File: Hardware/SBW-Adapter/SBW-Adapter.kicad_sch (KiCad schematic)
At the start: 5 parts, among them J1 JTAG, J2 SpyBiWire, SW1 SW_SPDT

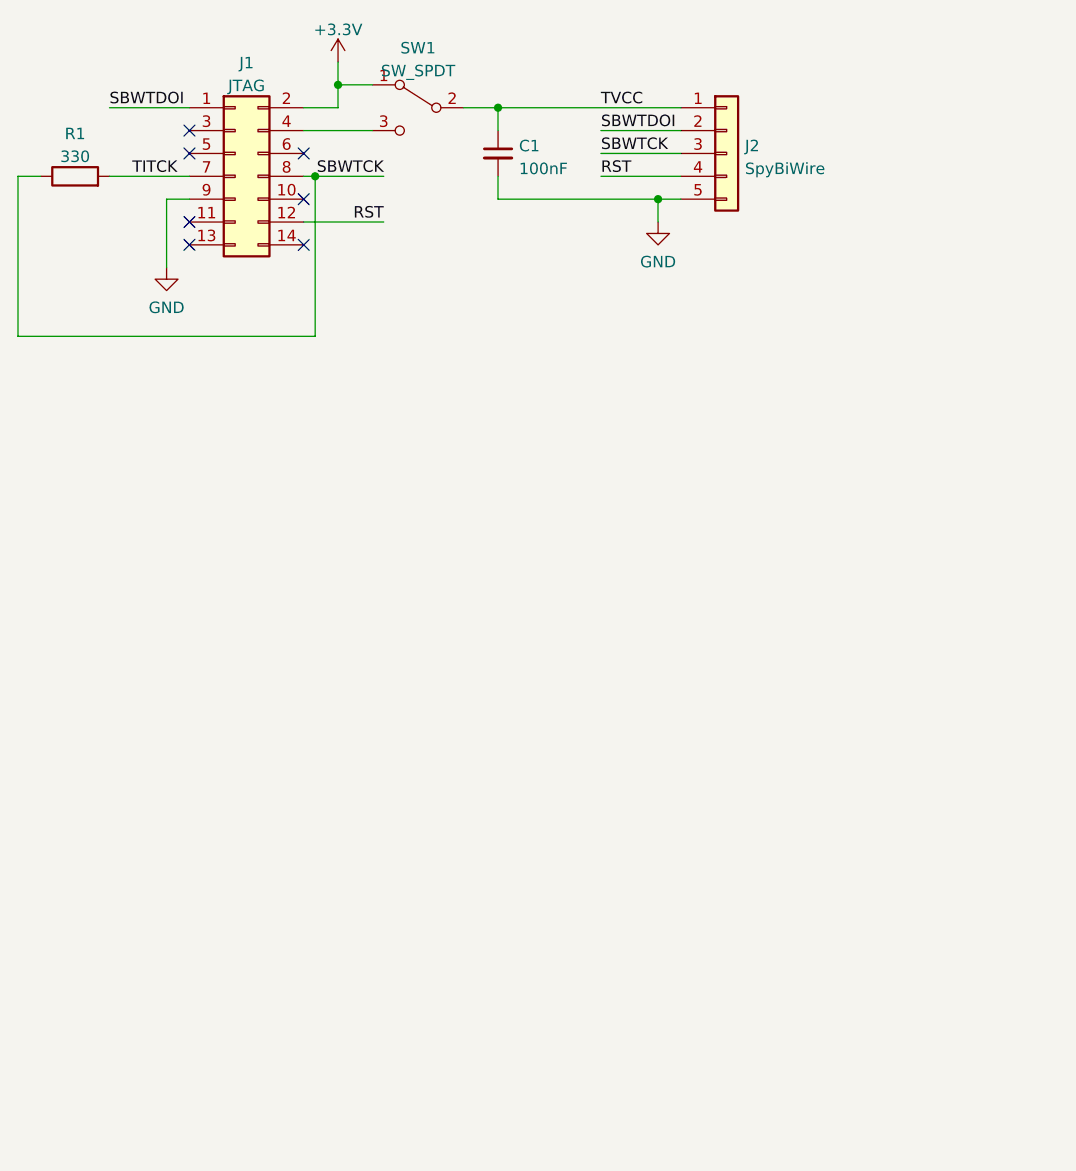
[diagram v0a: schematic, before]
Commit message: Files for PCB Manufacturing of 4 boards. Preparation for Board documentation
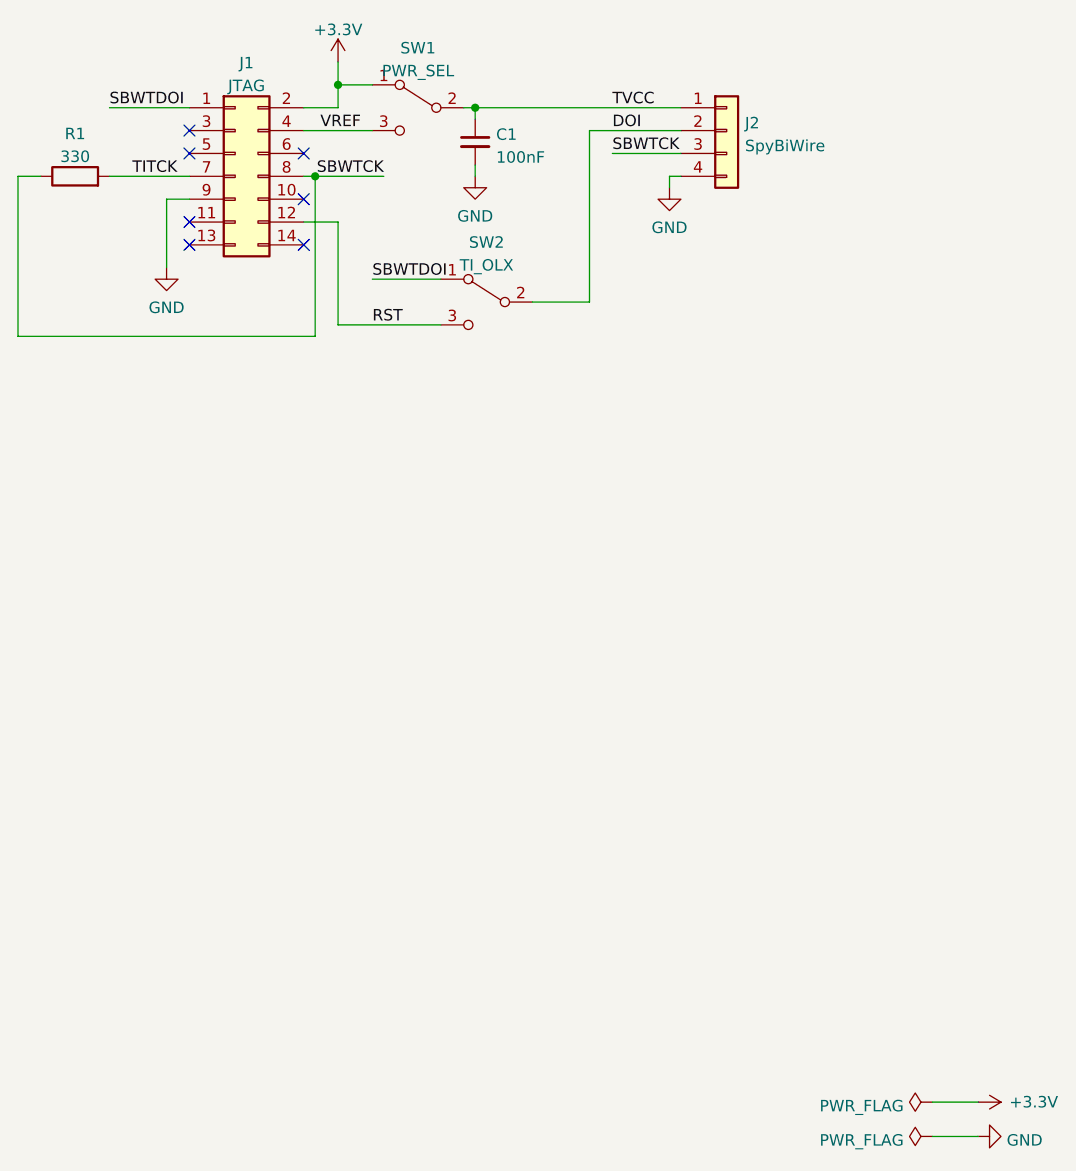
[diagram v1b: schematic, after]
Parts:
- added SW2: TI_OLX, Button_Switch_SMD:SW_SPDT_PCM12, symbol Switch:SW_SPDT
- J2: footprint Connector_PinHeader_2.54mm:PinHeader_1x05_P2.54mm_Horizontal -> Connector_JST:JST_XH_B4B-XH-A_1x04_P2.50mm_Vertical; symbol Connector_Generic:Conn_01x05 -> Connector_Generic:Conn_01x04
- SW1: value SW_SPDT -> PWR_SEL
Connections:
- net GND: now also J2.4 (Pin_4); no longer J2.5 (Pin_5)
- net RST: now also SW2.3 (C); no longer J2.4 (Pin_4)
- net SBWTDOI: now also SW2.1 (A); no longer J2.2 (Pin_2)
- net VREF: now reaches J1.4 (Pin_4), SW1.3 (C)
- new net DOI: J2.2 (Pin_2), SW2.2 (B)
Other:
- moved on the sheet: C1

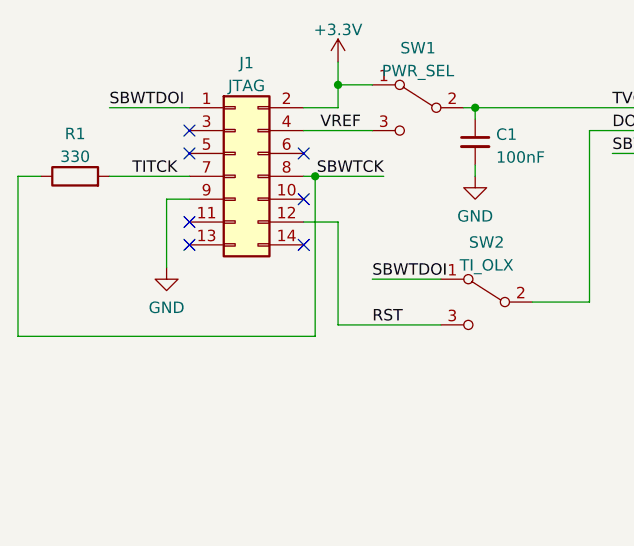
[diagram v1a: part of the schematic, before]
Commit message: Fixed an error on the Olimex SBW layout
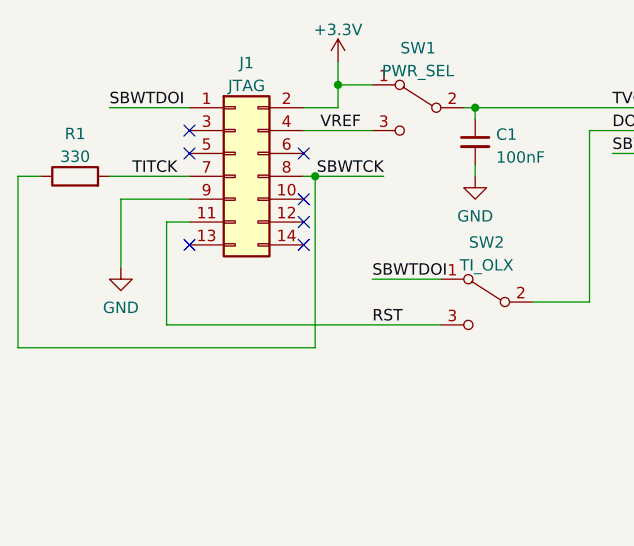
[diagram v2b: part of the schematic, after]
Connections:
- net RST: now also J1.11 (Pin_11); no longer J1.12 (Pin_12)
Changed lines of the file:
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@@
 (kicad_sch (version 20211123) (generator eeschema)
   (paper "A4")
+  (title_block
+    (date "2022-09-06")
+    (rev "2")
+  )
   (junction (at 87.63 85.09) (diameter 0) (color 0 0 0 0)
   )
@@
   )
   (no_connect (at 86.36 82.55))
+  (no_connect (at 86.36 90.17))
   (no_connect (at 86.36 87.63))
   (no_connect (at 86.36 92.71))
-  (no_connect (at 73.66 90.17))
   (no_connect (at 73.66 82.55))
   (no_connect (at 73.66 92.71))
@@
     (stroke (width 0) (type default) (color 0 0 0 0))
   )
+  (wire (pts (xy 71.12 101.6) (xy 101.6 101.6))
+    (stroke (width 0) (type default) (color 0 0 0 0))
+  )
   (wire (pts (xy 127 85.09) (xy 127 86.36))
     (stroke (width 0) (type default) (color 0 0 0 0))
@@
     (stroke (width 0) (type default) (color 0 0 0 0))
   )
-  (wire (pts (xy 73.66 87.63) (xy 71.12 87.63))
-    (stroke (width 0) (type default) (color 0 0 0 0))
-  )
-  (wire (pts (xy 54.61 102.87) (xy 54.61 85.09))
-    (stroke (width 0) (type default) (color 0 0 0 0))
-  )
-  (wire (pts (xy 87.63 102.87) (xy 54.61 102.87))
+  (wire (pts (xy 73.66 87.63) (xy 66.04 87.63))
+    (stroke (width 0) (type default) (color 0 0 0 0))
+  )
+  (wire (pts (xy 54.61 104.14) (xy 54.61 85.09))
+    (stroke (width 0) (type default) (color 0 0 0 0))
+  )
+  (wire (pts (xy 87.63 104.14) (xy 54.61 104.14))
     (stroke (width 0) (type default) (color 0 0 0 0))
   )
@@
     (stroke (width 0) (type default) (color 0 0 0 0))
   )
-  (wire (pts (xy 101.6 101.6) (xy 90.17 101.6))
-    (stroke (width 0) (type default) (color 0 0 0 0))
-  )
   (wire (pts (xy 90.17 74.93) (xy 93.98 74.93))
     (stroke (width 0) (type default) (color 0 0 0 0))
   )
-  (wire (pts (xy 86.36 90.17) (xy 90.17 90.17))
+  (wire (pts (xy 71.12 101.6) (xy 71.12 90.17))
     (stroke (width 0) (type default) (color 0 0 0 0))
   )
@@
     (stroke (width 0) (type default) (color 0 0 0 0))
   )
-  (wire (pts (xy 87.63 85.09) (xy 87.63 102.87))
-    (stroke (width 0) (type default) (color 0 0 0 0))
-  )
-  (wire (pts (xy 90.17 90.17) (xy 90.17 101.6))
+  (wire (pts (xy 87.63 85.09) (xy 87.63 104.14))
+    (stroke (width 0) (type default) (color 0 0 0 0))
+  )
+  (wire (pts (xy 71.12 90.17) (xy 73.66 90.17))
     (stroke (width 0) (type default) (color 0 0 0 0))
   )
@@
     (stroke (width 0) (type default) (color 0 0 0 0))
   )
-  (wire (pts (xy 71.12 87.63) (xy 71.12 95.25))
+  (wire (pts (xy 66.04 87.63) (xy 66.04 95.25))
     (stroke (width 0) (type default) (color 0 0 0 0))
   )
@@
     (pin "3")
   )
-  (symbol (lib_id "power:GND") (at 71.12 95.25 0) (unit 1)
-    (in_bom yes) (on_board yes) (fields_autoplaced)
-    (property "Reference" "#PWR0101" (id 0) (at 71.12 101.6 0)
-      (effects (font (size 1.27 1.27)) hide)
-    )
-    (property "Value" "GND" (id 1) (at 71.12 99.6934 0))
-    (property "Footprint" "" (id 2) (at 71.12 95.25 0)
-      (effects (font (size 1.27 1.27)) hide)
-    )
-    (property "Datasheet" "" (id 3) (at 71.12 95.25 0)
-      (effects (font (size 1.27 1.27)) hide)
-    )
+  (symbol (lib_id "power:GND") (at 66.04 95.25 0) (unit 1)
+    (in_bom yes) (on_board yes) (fields_autoplaced)
+    (property "Reference" "#PWR0101" (id 0) (at 66.04 101.6 0)
+      (effects (font (size 1.27 1.27)) hide)
+    )
+    (property "Value" "GND" (id 1) (at 66.04 99.6934 0))
+    (property "Footprint" "" (id 2) (at 66.04 95.25 0)
+      (effects (font (size 1.27 1.27)) hide)
+    )
+    (property "Datasheet" "" (id 3) (at 66.04 95.25 0)
+      (effects (font (size 1.27 1.27)) hide)
+    )

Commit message: Review of SBW-Adapter
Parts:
- SW1, SW2: footprint Button_Switch_SMD:SW_SPDT_PCM12 -> lib:SW_SPDT_PCM12; symbol Switch:SW_SPDT -> SW_SPDT_PCM12:SW_SPDT_PCM12
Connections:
- net GND: now also SW1.4 (GND), SW2.4 (GND)
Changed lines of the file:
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@@
   (paper "A4")
   (title_block
-    (date "2022-09-06")
+    (date "2022-12-08")
     (rev "2")
   )
@@
     (stroke (width 0) (type default) (color 0 0 0 0))
   )
+  (wire (pts (xy 106.68 105.41) (xy 106.68 106.68))
+    (stroke (width 0) (type default) (color 0 0 0 0))
+  )
   (wire (pts (xy 87.63 104.14) (xy 54.61 104.14))
     (stroke (width 0) (type default) (color 0 0 0 0))
@@
   )
   (wire (pts (xy 87.63 85.09) (xy 95.25 85.09))
+    (stroke (width 0) (type default) (color 0 0 0 0))
+  )
+  (wire (pts (xy 99.06 83.82) (xy 99.06 85.09))
     (stroke (width 0) (type default) (color 0 0 0 0))
   )
@@
   (symbol (lib_id "power:GND") (at 105.41 85.09 0) (unit 1)
     (in_bom yes) (on_board yes) (fields_autoplaced)
-    (property "Reference" "#PWR0103" (id 0) (at 105.41 91.44 0)
+    (property "Reference" "#PWR04" (id 0) (at 105.41 91.44 0)
       (effects (font (size 1.27 1.27)) hide)
     )
@@
   (symbol (lib_id "power:PWR_FLAG") (at 156.21 191.77 90) (unit 1)
     (in_bom yes) (on_board yes) (fields_autoplaced)
-    (property "Reference" "#FLG0102" (id 0) (at 154.305 191.77 0)
+    (property "Reference" "#FLG02" (id 0) (at 154.305 191.77 0)
       (effects (font (size 1.27 1.27)) hide)
     )
@@
     (pin "4")
   )
+  (symbol (lib_id "power:GND") (at 106.68 106.68 0) (unit 1)
+    (in_bom yes) (on_board yes) (fields_autoplaced)
+    (property "Reference" "#PWR05" (id 0) (at 106.68 113.03 0)
+      (effects (font (size 1.27 1.27)) hide)
+    )
+    (property "Value" "GND" (id 1) (at 106.68 111.1234 0))
+    (property "Footprint" "" (id 2) (at 106.68 106.68 0)
+      (effects (font (size 1.27 1.27)) hide)
+    )
+    (property "Datasheet" "" (id 3) (at 106.68 106.68 0)
+      (effects (font (size 1.27 1.27)) hide)
+    )
+    (pin "1")
+  )
+  (symbol (lib_id "power:GND") (at 99.06 85.09 0) (unit 1)
+    (in_bom yes) (on_board yes) (fields_autoplaced)
+    (property "Reference" "#PWR03" (id 0) (at 99.06 91.44 0)
+      (effects (font (size 1.27 1.27)) hide)
+    )
+    (property "Value" "GND" (id 1) (at 99.06 89.5334 0))
+    (property "Footprint" "" (id 2) (at 99.06 85.09 0)
+      (effects (font (size 1.27 1.27)) hide)
+    )
+    (property "Datasheet" "" (id 3) (at 99.06 85.09 0)
+      (effects (font (size 1.27 1.27)) hide)
+    )
+    (pin "1")
+  )
   (symbol (lib_id "power:+3.3V") (at 90.17 72.39 0) (unit 1)
     (in_bom yes) (on_board yes) (fields_autoplaced)
-    (property "Reference" "#PWR0102" (id 0) (at 90.17 76.2 0)
+    (property "Reference" "#PWR02" (id 0) (at 90.17 76.2 0)
       (effects (font (size 1.27 1.27)) hide)
     )
@@
   (symbol (lib_id "power:PWR_FLAG") (at 156.21 187.96 90) (unit 1)
     (in_bom yes) (on_board yes) (fields_autoplaced)
-    (property "Reference" "#FLG0101" (id 0) (at 154.305 187.96 0)
+    (property "Reference" "#FLG01" (id 0) (at 154.305 187.96 0)
       (effects (font (size 1.27 1.27)) hide)
     )
@@
   (symbol (lib_id "power:GND") (at 161.29 191.77 90) (unit 1)
     (in_bom yes) (on_board yes) (fields_autoplaced)
-    (property "Reference" "#PWR0104" (id 0) (at 167.64 191.77 0)
+    (property "Reference" "#PWR08" (id 0) (at 167.64 191.77 0)
       (effects (font (size 1.27 1.27)) hide)
     )
@@
   (symbol (lib_id "power:GND") (at 127 86.36 0) (unit 1)
     (in_bom yes) (on_board yes) (fields_autoplaced)
-    (property "Reference" "#PWR01" (id 0) (at 127 92.71 0)
+    (property "Reference" "#PWR06" (id 0) (at 127 92.71 0)
       (effects (font (size 1.27 1.27)) hide)
     )
@@
     (pin "2")
   )
-  (symbol (lib_id "Switch:SW_SPDT") (at 106.68 99.06 0) (mirror y) (unit 1)
-    (in_bom yes) (on_board yes) (fields_autoplaced)
-    (property "Reference" "SW2" (id 0) (at 106.68 92.4392 0))
-    (property "Value" "TI_OLX" (id 1) (at 106.68 94.9761 0))
-    (property "Footprint" "Button_Switch_SMD:SW_SPDT_PCM12" (id 2) (at 106.68 99.06 0)
+  (symbol (lib_id "SW_SPDT_PCM12:SW_SPDT_PCM12") (at 106.68 99.06 0) (mirror y) (unit 1)
+    (in_bom yes) (on_board yes)
+    (property "Reference" "SW2" (id 0) (at 111.76 96.52 0))
+    (property "Value" "TI_OLX" (id 1) (at 106.68 93.98 0))
+    (property "Footprint" "lib:SW_SPDT_PCM12" (id 2) (at 106.68 99.06 0)
       (effects (font (size 1.27 1.27)) hide)
     )
@@
     (pin "2")
     (pin "3")
+    (pin "4")
   )
   (symbol (lib_id "Device:R") (at 60.96 85.09 90) (unit 1)
@@
   (symbol (lib_id "power:+3.3V") (at 161.29 187.96 270) (unit 1)
     (in_bom yes) (on_board yes)
-    (property "Reference" "#PWR0105" (id 0) (at 157.48 187.96 0)
+    (property "Reference" "#PWR07" (id 0) (at 157.48 187.96 0)
       (effects (font (size 1.27 1.27)) hide)
     )
@@
     (pin "9")
   )
-  (symbol (lib_id "Switch:SW_SPDT") (at 99.06 77.47 0) (mirror y) (unit 1)
-    (in_bom yes) (on_board yes) (fields_autoplaced)
-    (property "Reference" "SW1" (id 0) (at 99.06 70.8492 0))
-    (property "Value" "PWR_SEL" (id 1) (at 99.06 73.3861 0))
-    (property "Footprint" "Button_Switch_SMD:SW_SPDT_PCM12" (id 2) (at 99.06 77.47 0)
+  (symbol (lib_id "SW_SPDT_PCM12:SW_SPDT_PCM12") (at 99.06 77.47 0) (mirror y) (unit 1)
+    (in_bom yes) (on_board yes)
+    (property "Reference" "SW1" (id 0) (at 104.14 74.93 0))
+    (property "Value" "PWR_SEL" (id 1) (at 99.06 72.39 0))
+    (property "Footprint" "lib:SW_SPDT_PCM12" (id 2) (at 99.06 77.47 0)
       (effects (font (size 1.27 1.27)) hide)
     )
@@
     (pin "2")
     (pin "3")
+    (pin "4")
   )
   (symbol (lib_id "power:GND") (at 66.04 95.25 0) (unit 1)
     (in_bom yes) (on_board yes) (fields_autoplaced)
-    (property "Reference" "#PWR0101" (id 0) (at 66.04 101.6 0)
+    (property "Reference" "#PWR01" (id 0) (at 66.04 101.6 0)
       (effects (font (size 1.27 1.27)) hide)
     )
@@
   (symbol_instances
     (path "/36efb54b-9261-4f54-bf1c-57d75ddbc017"
-      (reference "#FLG0101") (unit 1) (value "PWR_FLAG") (footprint "")
+      (reference "#FLG01") (unit 1) (value "PWR_FLAG") (footprint "")
     )
     (path "/06429605-ee59-42ff-919b-99089fdaa05b"
-      (reference "#FLG0102") (unit 1) (value "PWR_FLAG") (footprint "")
+      (reference "#FLG02") (unit 1) (value "PWR_FLAG") (footprint "")
+    )
+    (path "/e1f1dc11-5124-4b20-9cb4-841524384d96"
+      (reference "#PWR01") (unit 1) (value "GND") (footprint "")
+    )
+    (path "/36c1e10b-a056-457c-97f1-1254b0f646b2"
+      (reference "#PWR02") (unit 1) (value "+3.3V") (footprint "")
+    )
+    (path "/30757f9b-685b-4fbc-bc0b-b5b53555d6b8"
+      (reference "#PWR03") (unit 1) (value "GND") (footprint "")
+    )
+    (path "/01b04ce3-c619-48fb-a0ee-59db0667186e"
+      (reference "#PWR04") (unit 1) (value "GND") (footprint "")
+    )
+    (path "/2b91f2c0-f50a-432d-ae0c-eb3defc14040"
+      (reference "#PWR05") (unit 1) (value "GND") (footprint "")
     )
     (path "/51f2dc6a-ef8b-46b4-9a2a-486231c30300"
-      (reference "#PWR01") (unit 1) (value "GND") (footprint "")
-    )
-    (path "/e1f1dc11-5124-4b20-9cb4-841524384d96"
-      (reference "#PWR0101") (unit 1) (value "GND") (footprint "")
-    )
-    (path "/36c1e10b-a056-457c-97f1-1254b0f646b2"
-      (reference "#PWR0102") (unit 1) (value "+3.3V") (footprint "")
-    )
-    (path "/01b04ce3-c619-48fb-a0ee-59db0667186e"
-      (reference "#PWR0103") (unit 1) (value "GND") (footprint "")
+      (reference "#PWR06") (unit 1) (value "GND") (footprint "")
+    )
+    (path "/9ebb682f-1fbe-4cff-a2d5-696d3ab59137"
+      (reference "#PWR07") (unit 1) (value "+3.3V") (footprint "")
     )
     (path "/4be80805-2adf-40ca-be0a-740bf670f567"
-      (reference "#PWR0104") (unit 1) (value "GND") (footprint "")
-    )
-    (path "/9ebb682f-1fbe-4cff-a2d5-696d3ab59137"
-      (reference "#PWR0105") (unit 1) (value "+3.3V") (footprint "")
+      (reference "#PWR08") (unit 1) (value "GND") (footprint "")
     )
     (path "/5bab6b05-a84a-4a03-9a59-a57174307e88"
@@
     )
     (path "/bbc68c41-c6df-443e-a9f1-1531da9e0011"
-      (reference "SW1") (unit 1) (value "PWR_SEL") (footprint "Button_Switch_SMD:SW_SPDT_PCM12")
+      (reference "SW1") (unit 1) (value "PWR_SEL") (footprint "lib:SW_SPDT_PCM12")
     )
     (path "/698ca1d4-ae67-4385-af0d-5e514a845516"
-      (reference "SW2") (unit 1) (value "TI_OLX") (footprint "Button_Switch_SMD:SW_SPDT_PCM12")
-    )
-  )
+      (reference "SW2") (unit 1) (value "TI_OLX") (footprint "lib:SW_SPDT_PCM12")
+    )
+  )
